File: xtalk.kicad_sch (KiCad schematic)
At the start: 2 parts, among them J7 Conn_Coaxial

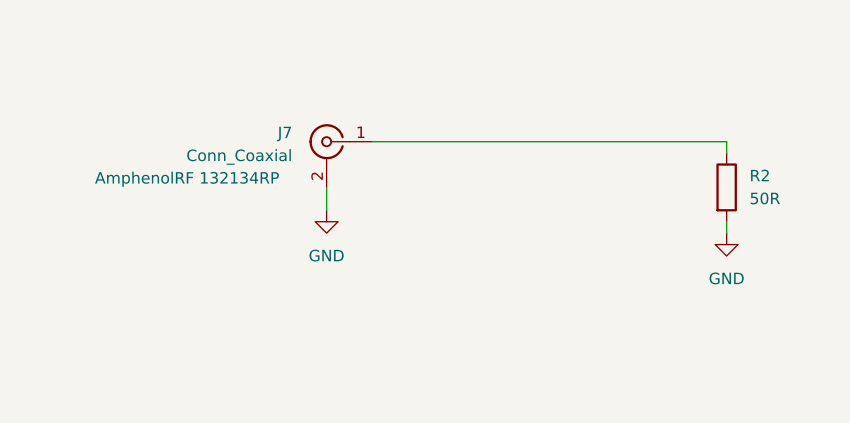
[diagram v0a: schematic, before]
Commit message: Rev B
Added 50R controlled Z, SOLT calibration and more reasonable tests
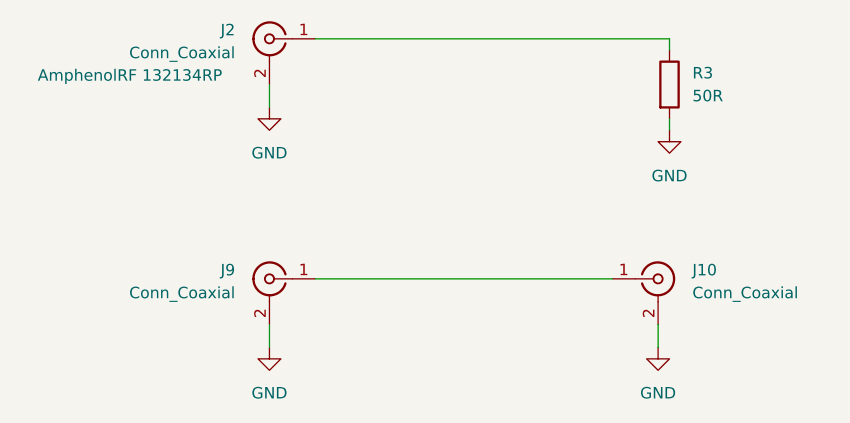
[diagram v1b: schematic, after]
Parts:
- removed J7: Conn_Coaxial, Library:SMA, symbol Connector:Conn_Coaxial
- removed R2: 50R, Resistor_SMD:R_0603_1608Metric, symbol Device:R
- added J10, J2, J9: Conn_Coaxial, Library:SMA, symbol Connector:Conn_Coaxial
- added R3: 50R, Resistor_SMD:R_0603_1608Metric, symbol Device:R
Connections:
- net GND: now also J10.2 (Ext), J2.2 (Ext), J9.2 (Ext), R3.2
- new net: J2.1 (In), R3.1
- new net: J10.1 (In), J9.1 (In)
